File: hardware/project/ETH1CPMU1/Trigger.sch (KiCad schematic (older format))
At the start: 17 parts, among them U1201 74AC125, U1202 ADuM5402

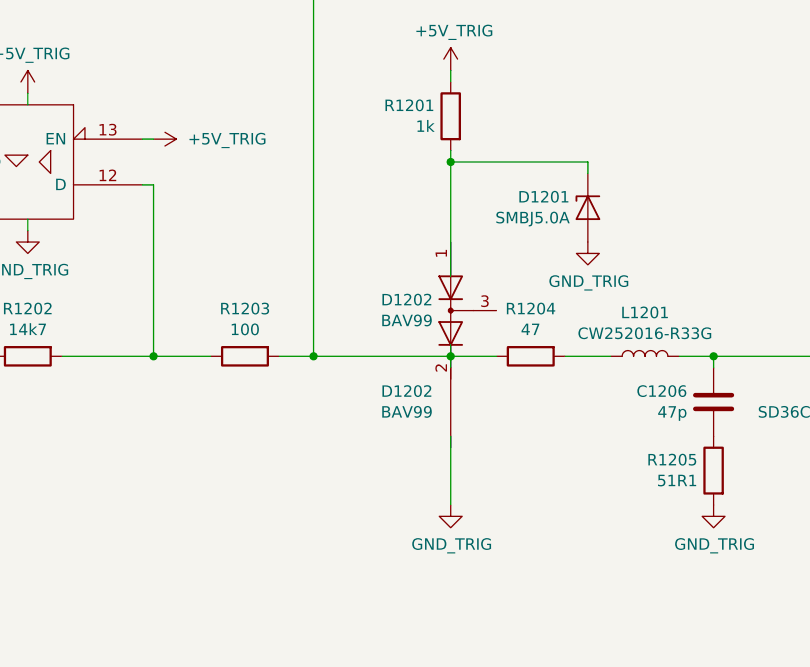
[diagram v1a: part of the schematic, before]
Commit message: Function generator schematic development.
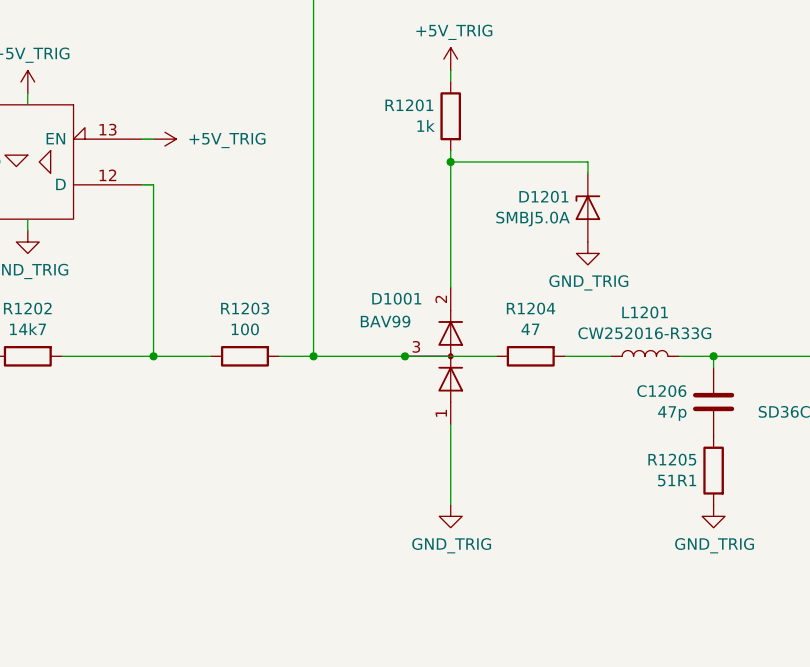
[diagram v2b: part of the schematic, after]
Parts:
- removed D1202: BAV99, Package_TO_SOT_SMD:SOT-23, symbol Diode:BAV99
- added D1001: BAV99, Package_TO_SOT_SMD:SOT-23, symbol Diode:BAV99
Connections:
- wire segments 92 -> 90
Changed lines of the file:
@@
 EESchema Schematic File Version 4
-LIBS:ETH1CPMU1-cache
 EELAYER 30 0
 EELAYER END
@@
 	8450 5450 8650 5450
 $Comp
-L Diode:BAV99 D1202
-U 1 1 5D1E5B75
-P 7950 5250
-F 0 "D1202" V 7904 5328 50  0000 L CNN
-F 1 "BAV99" V 7995 5328 50  0000 L CNN
-F 2 "Package_TO_SOT_SMD:SOT-23" H 7950 5100 50  0001 C CNN
-F 3 "https://assets.nexperia.com/documents/data-sheet/BAV99_SER.pdf" H 7950 5350 50  0001 C CNN
-	1    7950 5250
-	0    -1   1    0
-$EndComp
-Wire Wire Line
-	8150 5450 7950 5450
-Wire Wire Line
-	7950 5450 7950 5400
-Wire Wire Line
-	7950 5450 7950 5500
-Connection ~ 7950 5450
-Wire Wire Line
-	7950 6100 7950 5800
-$Comp
 L Device:D_Zener D1201
 U 1 1 5D1F1550
@@
 Wire Wire Line
 	8550 4600 7950 4600
-Wire Wire Line
-	7950 4600 7950 5100
 $Comp
 L Device:R R1201
@@
 Wire Wire Line
 	7950 4200 7950 4250
-Wire Wire Line
-	7950 5450 7350 5450
 $Comp
 L 74xx_IEEE:74125 U1201
@@
 Wire Wire Line
 	7200 5450 7350 5450
-Connection ~ 7350 5450
 Wire Wire Line
 	6100 4900 6100 4850
@@
 NoConn ~ 4200 3550
 $Comp
-L Diode:BAV99 D1202
-U 2 1 5D1E5E77
-P 7950 5650
-F 0 "D1202" V 7904 5728 50  0000 L CNN
-F 1 "BAV99" V 7995 5728 50  0000 L CNN
-F 2 "Package_TO_SOT_SMD:SOT-23" H 7950 5500 50  0001 C CNN
-F 3 "https://assets.nexperia.com/documents/data-sheet/BAV99_SER.pdf" H 7950 5750 50  0001 C CNN
-	2    7950 5650
-	0    -1   1    0
-$EndComp
-$Comp
 L power:+3.3V #PWR01207
 U 1 1 5EBBBCC5
@@
 	1    0    0    -1
 $EndComp
+$Comp
+L Diode:BAV99 D1001
+U 1 1 5DD77A27
+P 7950 5450
+F 0 "D1001" V 8200 5100 50  0000 L CNN
+F 1 "BAV99" V 8100 5050 50  0000 L CNN
+F 2 "Package_TO_SOT_SMD:SOT-23" H 7950 4950 50  0001 C CNN
+F 3 "https://assets.nexperia.com/documents/data-sheet/BAV99_SER.pdf" H 7950 5450 50  0001 C CNN
+	1    7950 5450
+	0    1    -1   0
+$EndComp
+Wire Wire Line
+	7750 5450 7350 5450
+Connection ~ 7350 5450
+Wire Wire Line
+	8150 5450 7750 5450
+Connection ~ 7750 5450
+Wire Wire Line
+	7950 4600 7950 5150
+Wire Wire Line
+	7950 5750 7950 6100
 $EndSCHEMATC

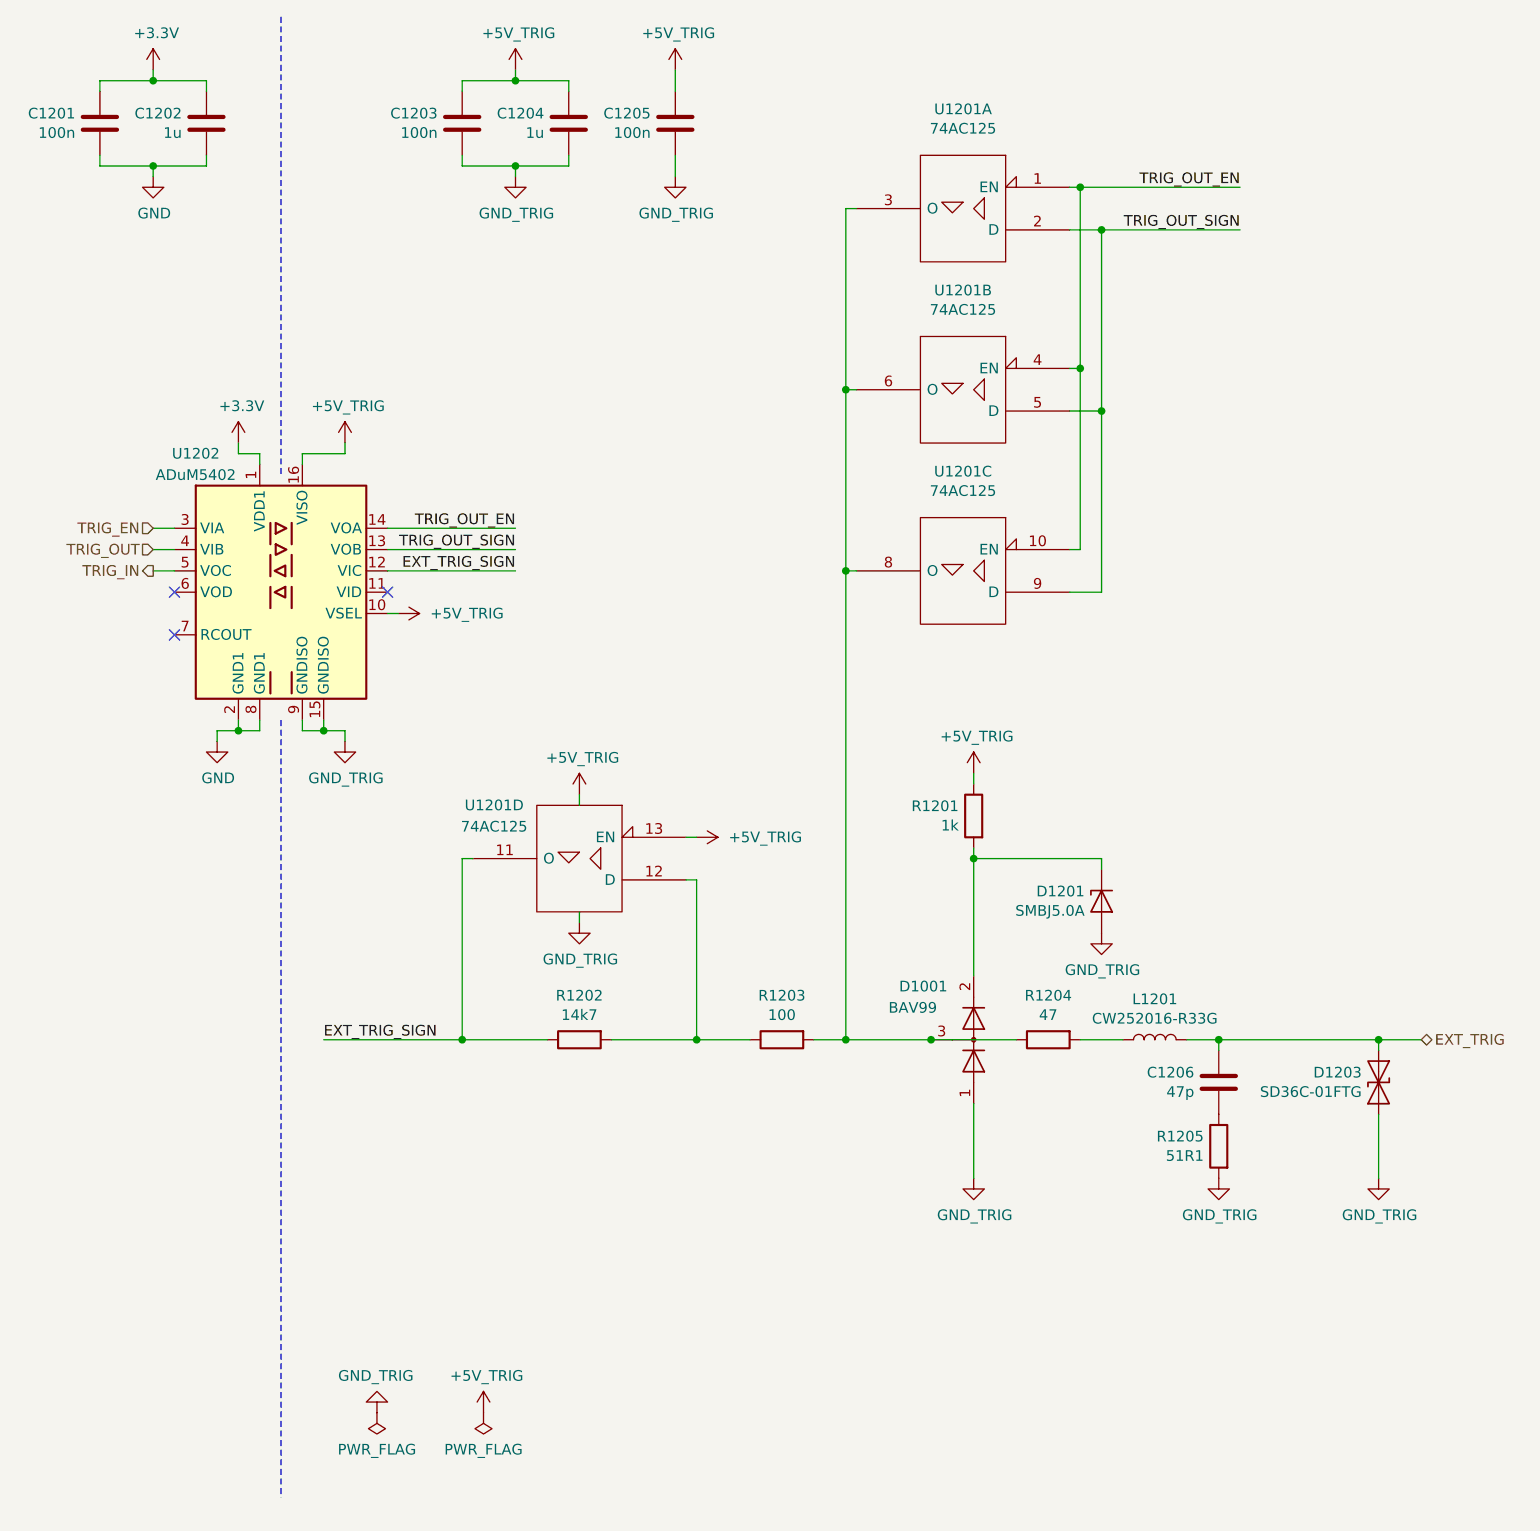
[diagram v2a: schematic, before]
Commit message: New footprint development, changes in schematics.
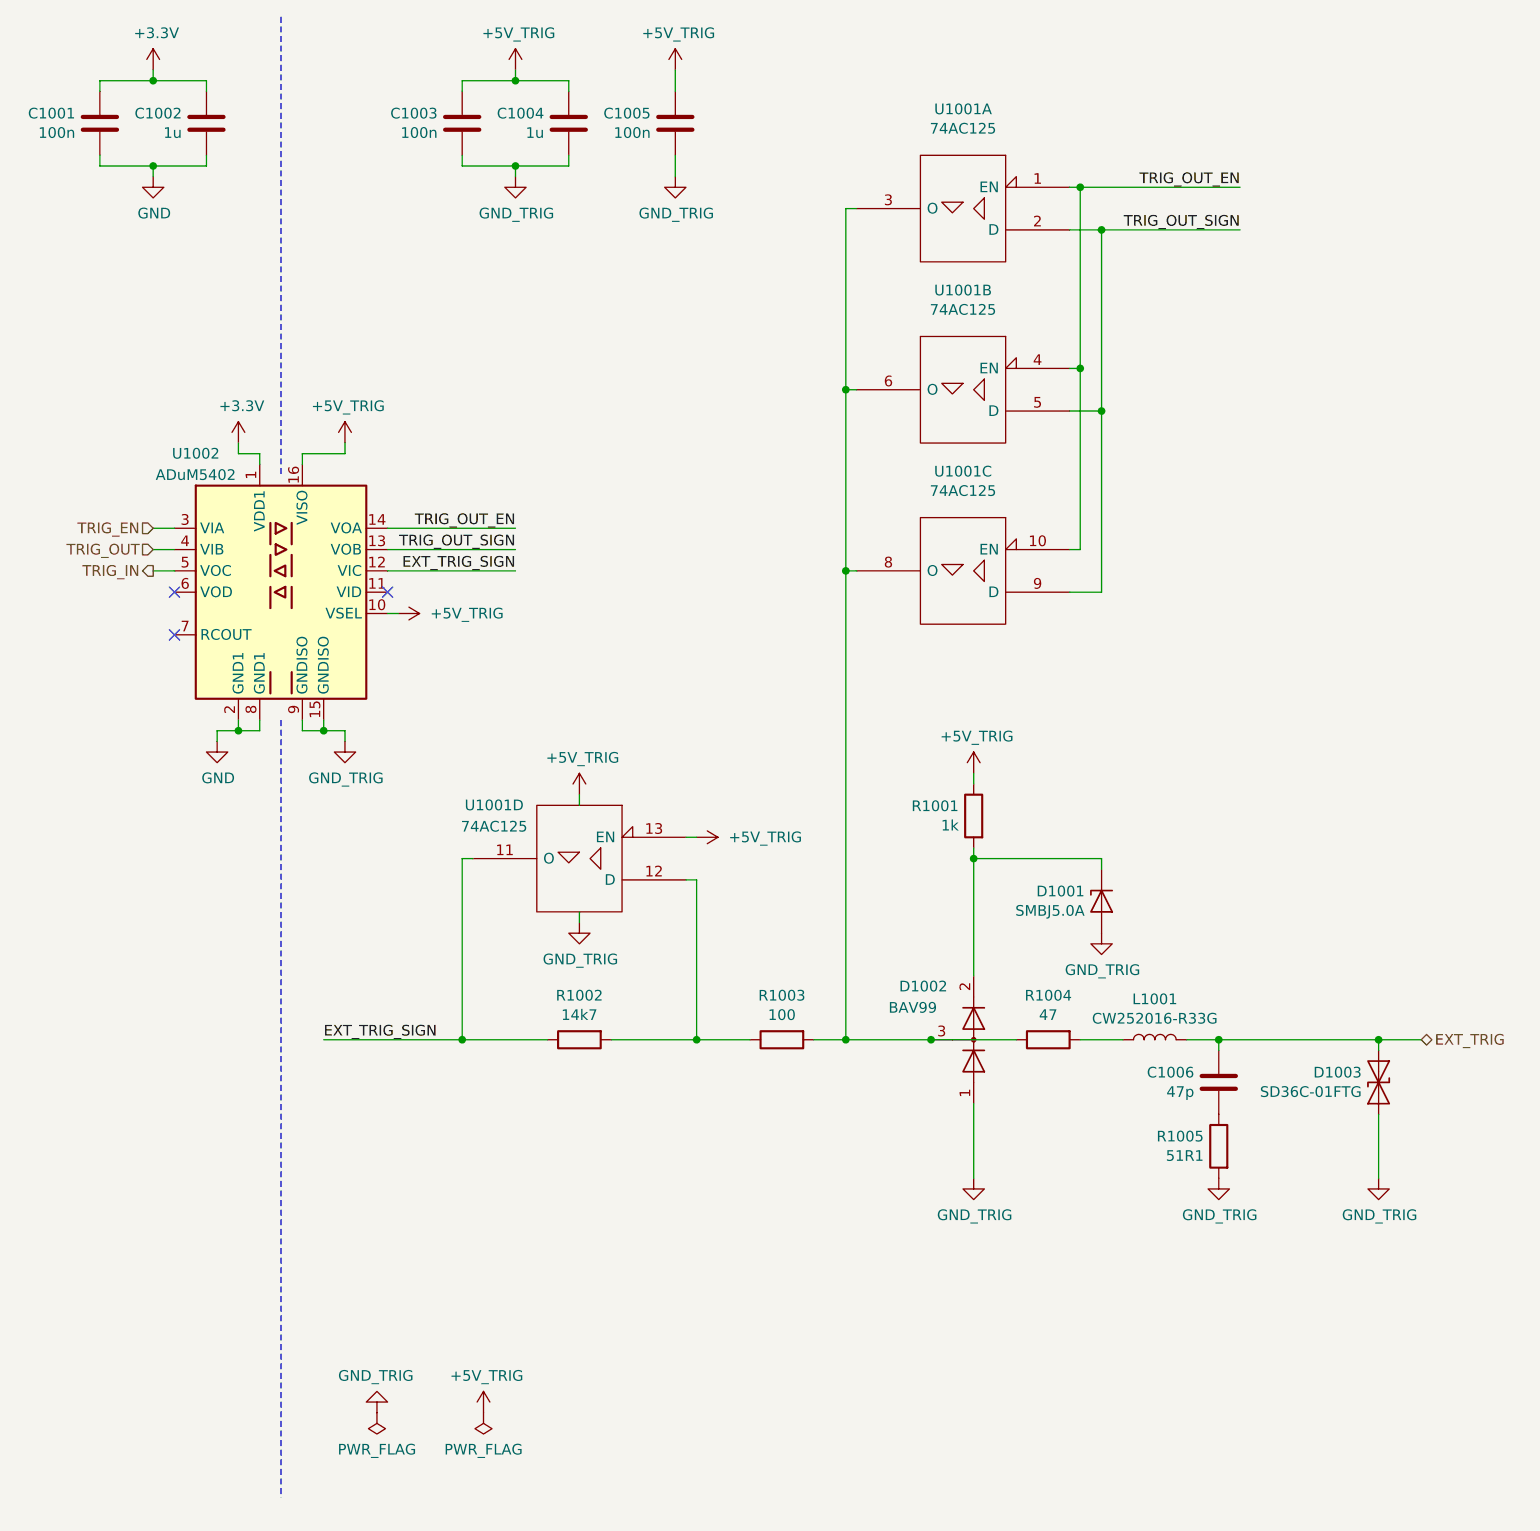
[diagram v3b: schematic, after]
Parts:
- C1001: renamed from C1201; footprint ETH1CJTAG:C_0603_A_Pad1.05x0.95mm_HandSolder -> Capacitor_SMD:C_0603_1608Metric_Pad1.05x0.95mm_HandSolder
- C1002: renamed from C1202; footprint ETH1CJTAG:C_0603_T_Pad1.05x0.95mm_HandSolder -> Capacitor_SMD:C_0603_1608Metric_Pad1.05x0.95mm_HandSolder
- C1003: renamed from C1203; footprint ETH1CJTAG:C_0603_A_Pad1.05x0.95mm_HandSolder -> Capacitor_SMD:C_0603_1608Metric_Pad1.05x0.95mm_HandSolder
- C1004: renamed from C1204; footprint ETH1CJTAG:C_0603_T_Pad1.05x0.95mm_HandSolder -> Capacitor_SMD:C_0603_1608Metric_Pad1.05x0.95mm_HandSolder
- C1005: renamed from C1205; footprint ETH1CJTAG:C_0603_A_Pad1.05x0.95mm_HandSolder -> Capacitor_SMD:C_0603_1608Metric_Pad1.05x0.95mm_HandSolder
- R1001: renamed from R1201; footprint ETH1CJTAG:R_0603_P_Pad1.05x0.95mm_HandSolder -> Resistor_SMD:R_0603_1608Metric_Pad1.05x0.95mm_HandSolder
- renumbered C1206 to C1006, D1201 to D1001, D1001 to D1002, D1203 to D1003, L1201 to L1001, R1202 to R1002, R1203 to R1003, R1204 to R1004, R1205 to R1005, U1201 to U1001, U1202 to U1002

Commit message: Schematic and PCB design.
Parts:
- added unit 5 of U1001
- L1001: footprint ETH1CJTAG:CW252016 -> ETH1CPMU1:CW252016
- U1001: symbol 74xx_IEEE:74125 -> ETH1CPMU1:74AC125
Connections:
- net +5V_TRIG: now also U1001.14 (VCC); no longer U1001.14 (VCC), U1001.14 (VCC), U1001.14 (VCC), U1001.14 (VCC)
- net GND: no longer C1003.2, C1004.2, C1005.2, D1001.2 (A), D1002.1 (K), D1003.2 (A2), R1005.2, U1001.7 (GND), U1001.7 (GND), U1001.7 (GND), U1001.7 (GND), U1002.15 (GNDISO), U1002.9 (GNDISO)
- new net GND_TRIG: C1003.2, C1004.2, C1005.2, D1001.2 (A), D1002.1 (K), D1003.2 (A2), R1005.2, U1001.7 (GND), U1002.15 (GNDISO), U1002.9 (GNDISO)
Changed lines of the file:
@@
 	4800 2700 4800 2750
 $Comp
-L 74xx_IEEE:74125 U1001
+L ETH1CPMU1:74AC125 U1001
 U 3 1 5D9C7DE2
 P 7900 3250
@@
 F 0 "L1001" V 8990 5450 50  0000 C CNN
 F 1 "CW252016-R33G" V 8899 5450 50  0000 C CNN
-F 2 "ETH1CJTAG:CW252016" H 8800 5450 50  0001 C CNN
+F 2 "ETH1CPMU1:CW252016" H 8800 5450 50  0001 C CNN
 F 3 "~" H 8800 5450 50  0001 C CNN
 	1    8800 5450
@@
 	7950 4200 7950 4250
 $Comp
-L 74xx_IEEE:74125 U1001
+L ETH1CPMU1:74AC125 U1001
 U 4 1 5D218310
 P 6100 4600
@@
 $EndComp
 $Comp
-L 74xx_IEEE:74125 U1001
+L ETH1CPMU1:74AC125 U1001
 U 2 1 5D2189A9
 P 7900 2400
@@
 $EndComp
 $Comp
-L 74xx_IEEE:74125 U1001
+L ETH1CPMU1:74AC125 U1001
 U 1 1 5D21AD13
 P 7900 1550
@@
 Wire Wire Line
 	7200 5450 7350 5450
-Wire Wire Line
-	6100 4900 6100 4850
-Wire Wire Line
-	6100 4300 6100 4350
 Wire Wire Line
 	6650 4500 6600 4500
@@
 $EndComp
 $Comp
-L ETH1CPMU1:GND_TRIG #PWR01015
-U 1 1 5EBDC368
-P 6100 4900
-F 0 "#PWR01015" H 6100 4650 50  0001 C CNN
-F 1 "GND_TRIG" H 6105 4727 50  0000 C CNN
-F 2 "" H 6100 4900 50  0001 C CNN
-F 3 "" H 6100 4900 50  0001 C CNN
-	1    6100 4900
-	1    0    0    -1
-$EndComp
-$Comp
 L ETH1CPMU1:GND_TRIG #PWR01017
 U 1 1 5EBDCCC1
@@
 F 3 "" H 5000 2650 50  0001 C CNN
 	1    5000 2650
-	1    0    0    -1
-$EndComp
-$Comp
-L ETH1CPMU1:+5V_TRIG #PWR01013
-U 1 1 5EBE5407
-P 6100 4300
-F 0 "#PWR01013" H 6100 4150 50  0001 C CNN
-F 1 "+5V_TRIG" H 6115 4473 50  0000 C CNN
-F 2 "" H 6100 4300 50  0001 C CNN
-F 3 "" H 6100 4300 50  0001 C CNN
-	1    6100 4300
 	1    0    0    -1
 $EndComp
@@
 $EndComp
 $Comp
-L power:PWR_FLAG #FLG01001
-U 1 1 5EC001F9
-P 5150 7200
-F 0 "#FLG01001" H 5150 7275 50  0001 C CNN
-F 1 "PWR_FLAG" H 5150 7373 50  0000 C CNN
-F 2 "" H 5150 7200 50  0001 C CNN
-F 3 "~" H 5150 7200 50  0001 C CNN
-	1    5150 7200
-	-1   0    0    1
-$EndComp
-$Comp
-L power:PWR_FLAG #FLG01002
-U 1 1 5EC00672
-P 5650 7200
-F 0 "#FLG01002" H 5650 7275 50  0001 C CNN
-F 1 "PWR_FLAG" H 5650 7373 50  0000 C CNN
-F 2 "" H 5650 7200 50  0001 C CNN
-F 3 "~" H 5650 7200 50  0001 C CNN
-	1    5650 7200
-	-1   0    0    1
-$EndComp
-$Comp
-L ETH1CPMU1:GND_TRIG #PWR01020
-U 1 1 5EC00B44
-P 5150 7200
-F 0 "#PWR01020" H 5150 6950 50  0001 C CNN
-F 1 "GND_TRIG" H 5155 7027 50  0000 C CNN
-F 2 "" H 5150 7200 50  0001 C CNN
-F 3 "" H 5150 7200 50  0001 C CNN
-	1    5150 7200
-	-1   0    0    1
-$EndComp
-$Comp
-L ETH1CPMU1:+5V_TRIG #PWR01021
-U 1 1 5EC0371C
-P 5650 7200
-F 0 "#PWR01021" H 5650 7050 50  0001 C CNN
-F 1 "+5V_TRIG" H 5665 7373 50  0000 C CNN
-F 2 "" H 5650 7200 50  0001 C CNN
-F 3 "" H 5650 7200 50  0001 C CNN
-	1    5650 7200
-	1    0    0    -1
-$EndComp
-$Comp
 L Diode:BAV99 D1002
 U 1 1 5DD77A27
@@
 Wire Wire Line
 	7950 5750 7950 6100
+$Comp
+L ETH1CPMU1:74AC125 U1001
+U 5 1 5E72A776
+P 5500 6850
+F 0 "U1001" H 5100 6950 50  0000 C CNN
+F 1 "74AC125" H 5100 6800 50  0000 C CNN
+F 2 "Package_SO:TSSOP-14_4.4x5mm_P0.65mm" H 5500 6850 50  0001 C CNN
+F 3 "" H 5500 6850 50  0001 C CNN
+	5    5500 6850
+	-1   0    0    -1
+$EndComp
+$Comp
+L ETH1CPMU1:+5V_TRIG #PWR01013
+U 1 1 5E72EC8D
+P 5500 6500
+F 0 "#PWR01013" H 5500 6350 50  0001 C CNN
+F 1 "+5V_TRIG" H 5515 6673 50  0000 C CNN
+F 2 "" H 5500 6500 50  0001 C CNN
+F 3 "" H 5500 6500 50  0001 C CNN
+	1    5500 6500
+	1    0    0    -1
+$EndComp
+$Comp
+L ETH1CPMU1:GND_TRIG #PWR01015
+U 1 1 5E7300C2
+P 5500 7200
+F 0 "#PWR01015" H 5500 6950 50  0001 C CNN
+F 1 "GND_TRIG" H 5505 7027 50  0000 C CNN
+F 2 "" H 5500 7200 50  0001 C CNN
+F 3 "" H 5500 7200 50  0001 C CNN
+	1    5500 7200
+	1    0    0    -1
+$EndComp
 $EndSCHEMATC

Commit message: Schematic design
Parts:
- renumbered C1001 to C801, C1002 to C802, C1003 to C803, C1004 to C804, C1005 to C805, C1006 to C806, D1001 to D801, D1002 to D802, D1003 to D803, L1001 to L801, R1001 to R801, R1002 to R802, R1003 to R803, R1004 to R804, R1005 to R805, U1001 to U801, U1002 to U802
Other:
- moved on the sheet: U801E
